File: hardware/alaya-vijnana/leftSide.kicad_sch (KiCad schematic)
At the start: 45 parts, among them J1 Bat, J2 USB_C_Receptacle_USB2.0_16P, U1 nRF52840, U2 BQ24075RGT, U3 XC6220B331MR, X1 32.768kHz, Y1 32Mhz

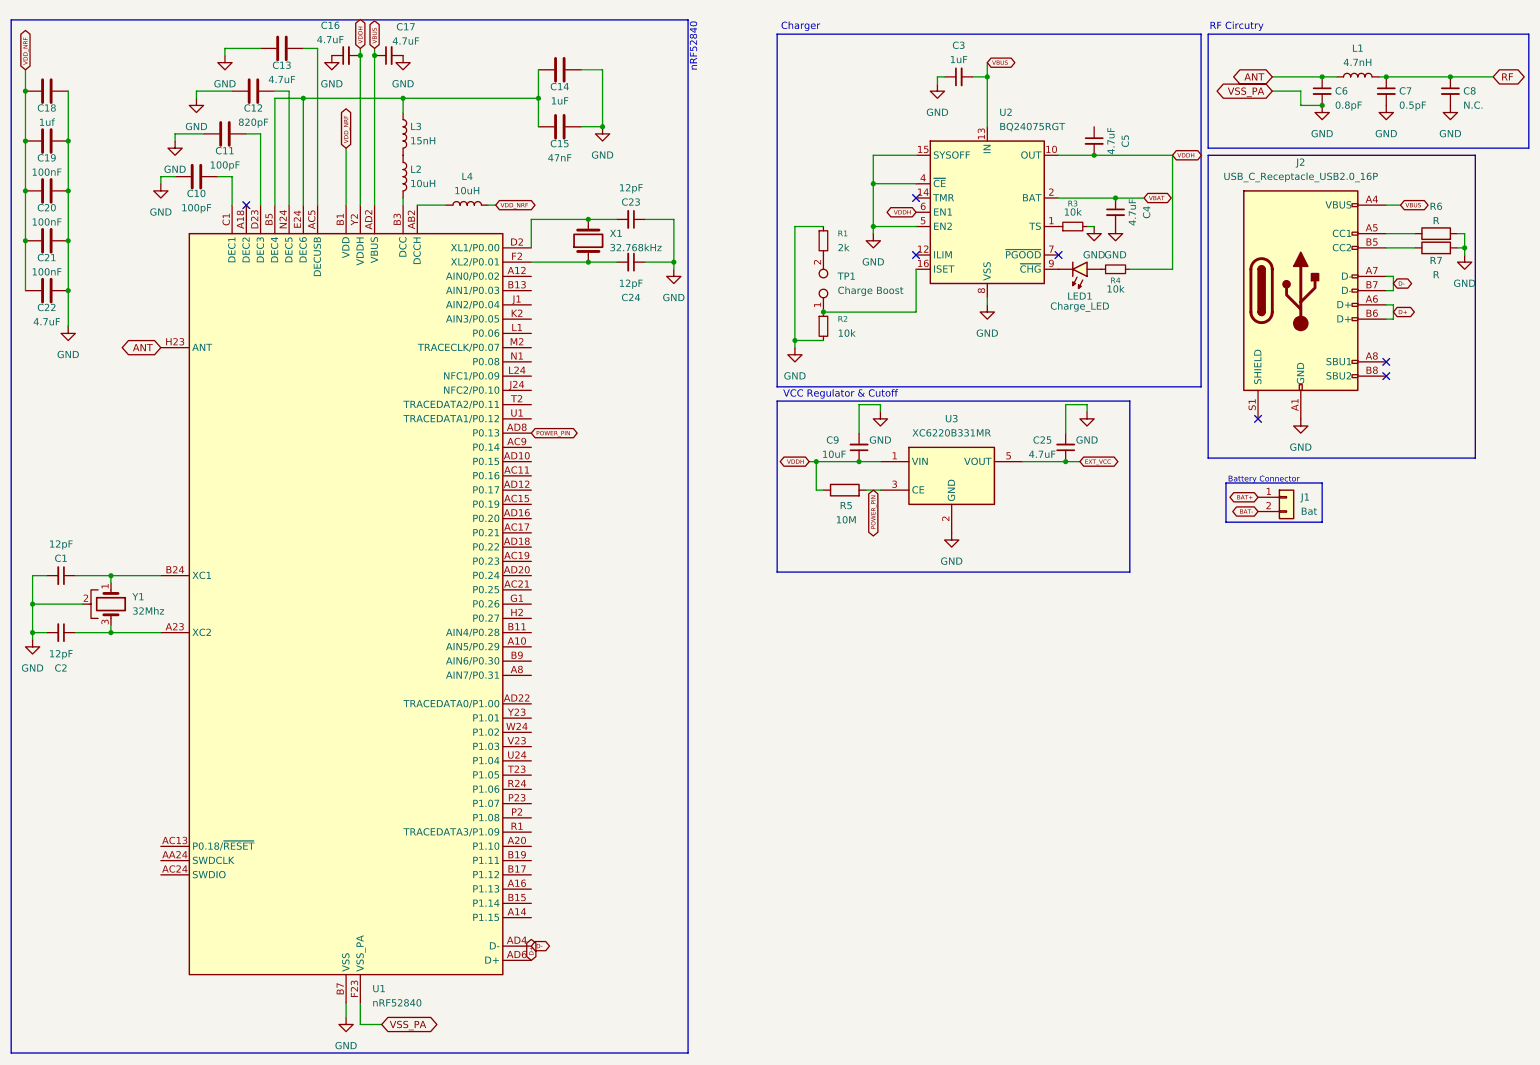
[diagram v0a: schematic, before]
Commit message: schematics done outside of cluster to main connectors, PCB laid out
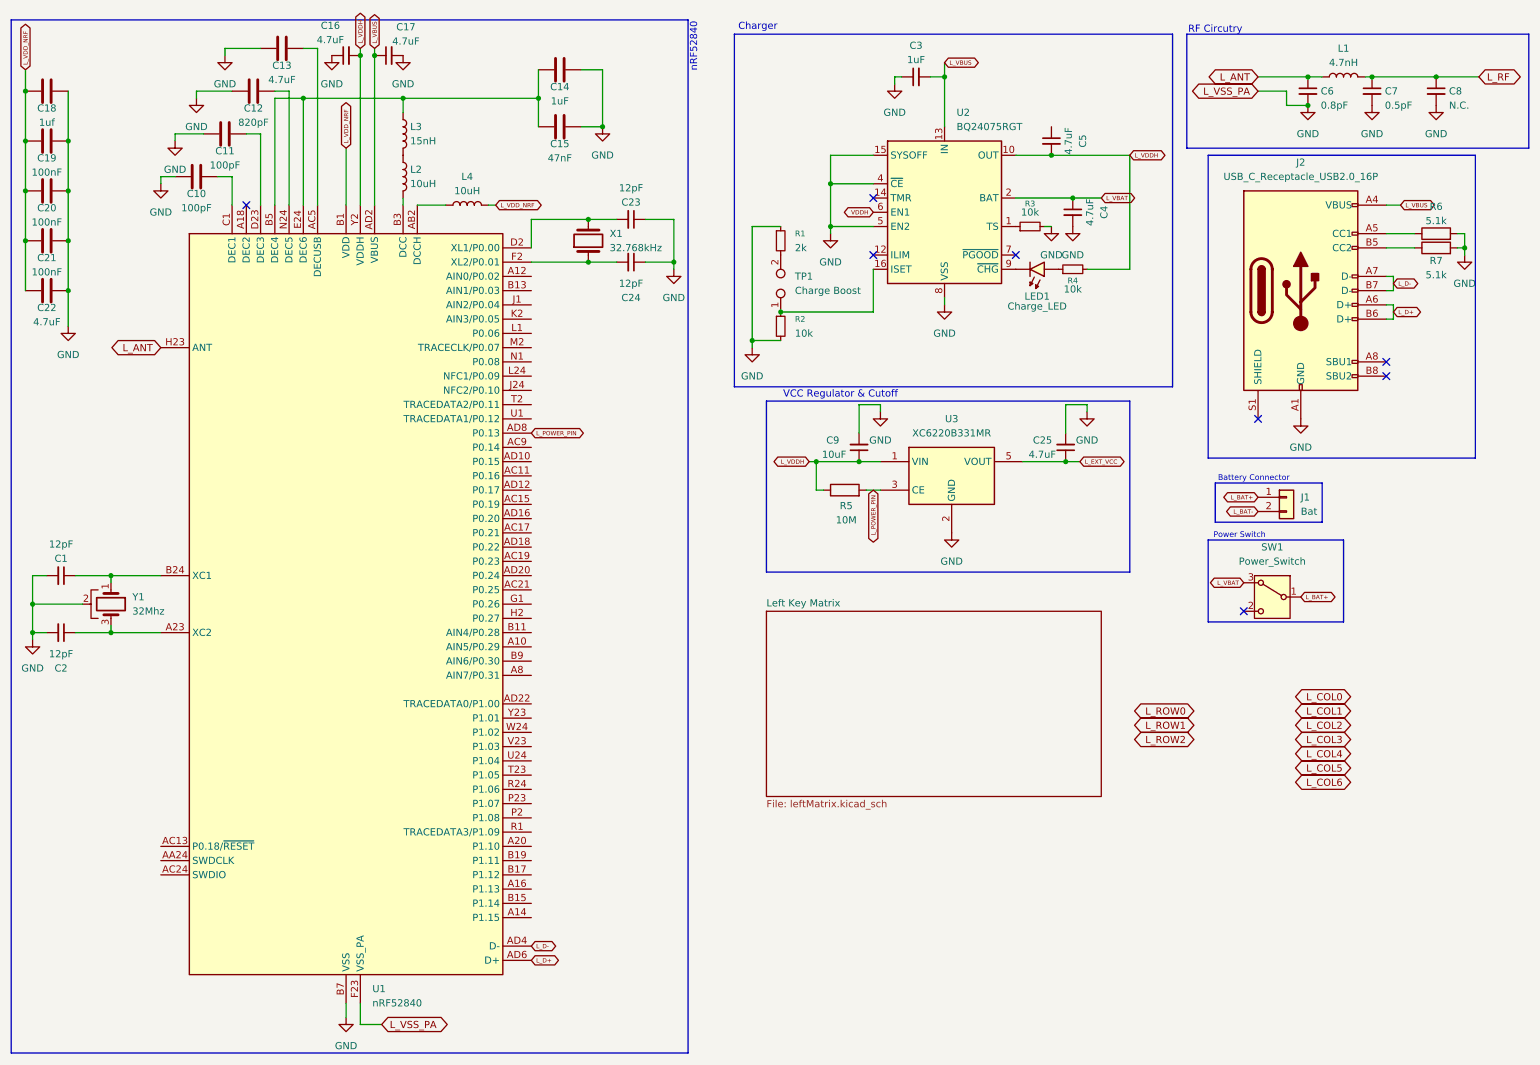
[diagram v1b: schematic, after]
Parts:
- added SW1: Power_Switch, Button_Switch_THT:SW_E-Switch_EG1224_SPDT_Angled, symbol Switch:SW_Wuerth_450301014042
- C1, C10, C11, C12, C13, C14, C15, C16, C17, C18, C19, C2, C20, C21, C22, C23, C24, C25, C3, C4, C5, C6, C7, C8, C9: footprint (none) -> Capacitor_SMD:C_0603_1608Metric_Pad1.08x0.95mm_HandSolder
- J2: footprint (none) -> Connector_USB:USB_C_Receptacle_GCT_USB4085
- L1: footprint (none) -> Inductor_SMD:L_0402_1005Metric_Pad0.77x0.64mm_HandSolder
- L2, L3, L4: footprint (none) -> Inductor_SMD:L_0603_1608Metric
- R1, R2, R3, R4, R5: footprint (none) -> Resistor_SMD:R_0603_1608Metric_Pad0.98x0.95mm_HandSolder
- R6, R7: value R -> 5.1k; footprint (none) -> Resistor_SMD:R_0603_1608Metric_Pad0.98x0.95mm_HandSolder
- TP1: footprint Connector_PinHeader_2.00mm:PinHeader_1x02_P2.00mm_Horizontal -> Resistor_SMD:R_2816_7142Metric_Pad3.20x4.45mm_HandSolder
- X1: footprint (none) -> Crystal:Crystal_SMD_2012-2Pin_2.0x1.2mm
- Y1: footprint (none) -> Crystal:Crystal_SMD_3225-4Pin_3.2x2.5mm_HandSoldering
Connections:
- net VDDH: no longer C16.2, C5.2, C9.1, R4.2, R5.1, U1.Y2 (VDDH), U2.10 (OUT), U2.11 (OUT), U3.1 (VIN)
- net ANT renamed L_ANT
- net BAT+ renamed L_BAT+
- net L_BAT+: now also SW1.1 (B)
- net BAT- renamed L_BAT-
- net D+ renamed L_D+
- net D- renamed L_D-
- net EXT_VCC renamed L_EXT_VCC
- net POWER_PIN renamed L_POWER_PIN
- net RF renamed L_RF
- net VBAT renamed L_VBAT
- net L_VBAT: now also SW1.3 (A)
- net VBUS renamed L_VBUS
- net VDD_NRF renamed L_VDD_NRF
- new net L_VDDH: C16.2, C5.2, C9.1, R4.2, R5.1, U1.Y2 (VDDH), U2.10 (OUT), U2.11 (OUT), U3.1 (VIN)
- no-connect marks 7 -> 8
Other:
- added sheet Left Key Matrix (leftMatrix.kicad_sch)
- note added: "Power Switch"
- moved on the sheet: C3, C4, C5, C6, C7, C8, L1, LED1, R1, R2, R3, R4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

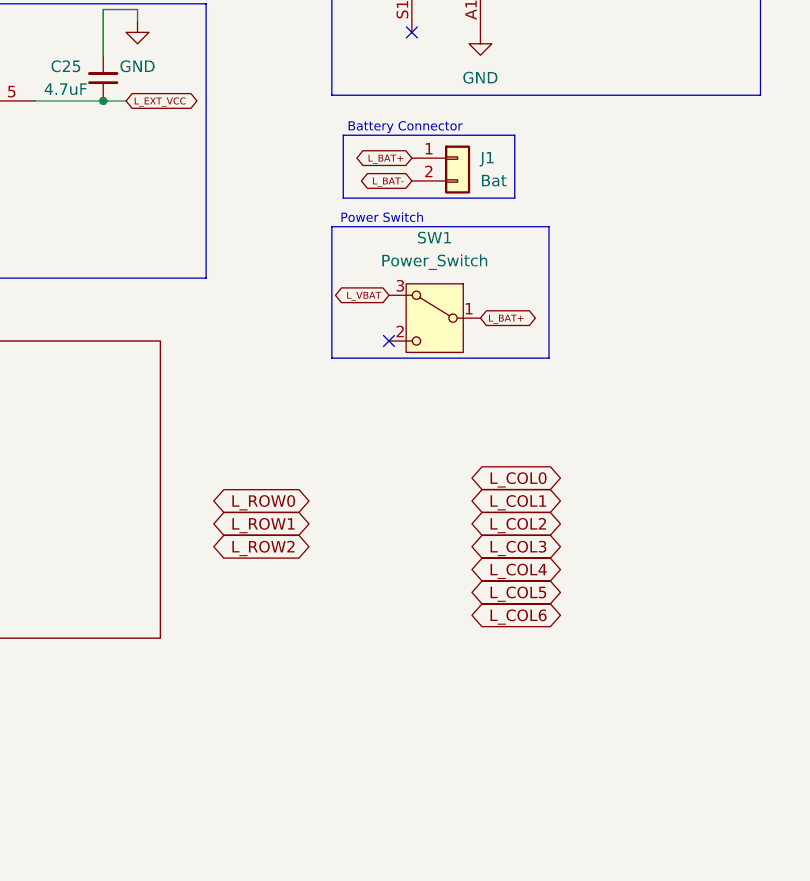
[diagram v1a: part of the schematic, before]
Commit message: finished key wiring w/ connectors
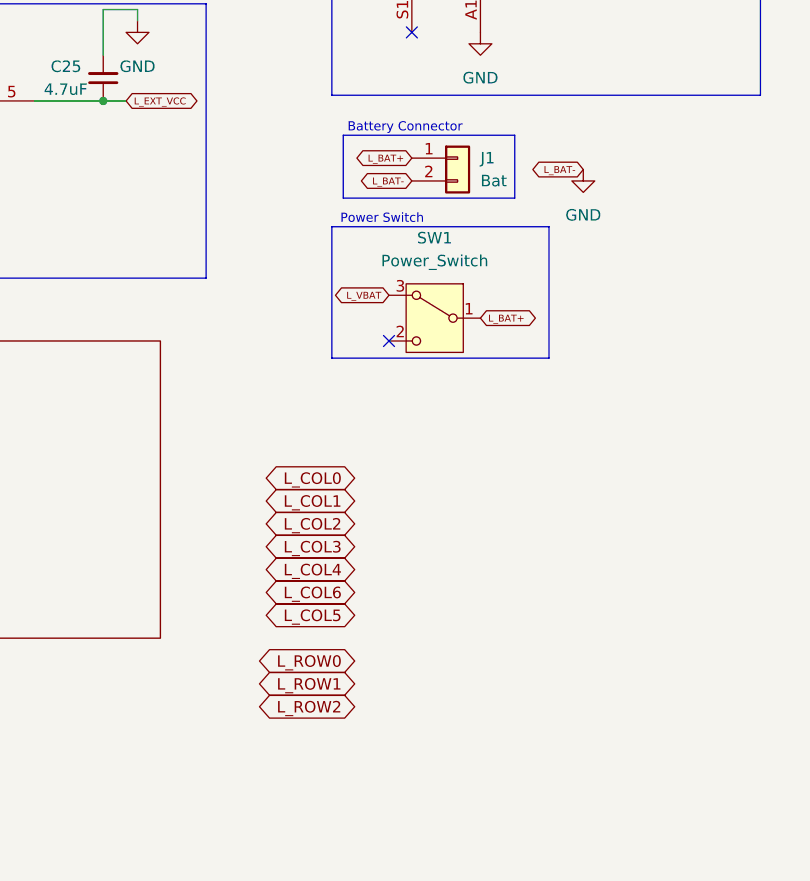
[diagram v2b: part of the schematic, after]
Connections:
- net L_BAT- is gone; now on net GND: J1.2 (Pin_2)
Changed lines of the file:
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@@
 		)
 	)
-	(global_label "L_ROW1"
+	(global_label "L_POWER_PIN"
 		(shape bidirectional)
-		(at 223.52 138.43 180)
+		(at 166.37 96.52 270)
 		(fields_autoplaced yes)
 		(effects
 			(font
-				(size 1.27 1.27)
+				(size 0.762 0.762)
 			)
 			(justify right)
 		)
 		(property "Intersheetrefs" "${INTERSHEET_REFS}"
-			(at 212.1664 138.43 0)
+			(at 166.37 106.5621 90)
 			(effects
 				(font
@@
 		)
 	)
-	(global_label "L_COL5"
+	(global_label "L_VDDH"
 		(shape bidirectional)
-		(at 251.46 146.05 180)
+		(at 212.09 36.83 0)
 		(fields_autoplaced yes)
 		(effects
 			(font
-				(size 1.27 1.27)
+				(size 0.762 0.762)
 			)
-			(justify right)
+			(justify left)
 		)
 		(property "Intersheetrefs" "${INTERSHEET_REFS}"
-			(at 240.5297 146.05 0)
+			(at 218.7211 36.83 0)
 			(effects
 				(font
 					(size 1.27 1.27)
 				)
-				(justify right)
+				(justify left)
 				(hide yes)
 			)
 		)
 	)
-	(global_label "L_POWER_PIN"
+	(global_label "L_ROW2"
 		(shape bidirectional)
-		(at 166.37 96.52 270)
+		(at 228.6 158.75 180)
 		(fields_autoplaced yes)
 		(effects
 			(font
-				(size 0.762 0.762)
+				(size 1.27 1.27)
 			)
 			(justify right)
 		)
 		(property "Intersheetrefs" "${INTERSHEET_REFS}"
-			(at 166.37 106.5621 90)
+			(at 217.2464 158.75 0)
 			(effects
 				(font
@@
 		)
 	)
-	(global_label "L_VDDH"
-		(shape bidirectional)
-		(at 212.09 36.83 0)
-		(fields_autoplaced yes)
-		(effects
-			(font
-				(size 0.762 0.762)
-			)
-			(justify left)
-		)
-		(property "Intersheetrefs" "${INTERSHEET_REFS}"
-			(at 218.7211 36.83 0)
-			(effects
-				(font
-					(size 1.27 1.27)
-				)
-				(justify left)
-				(hide yes)
-			)
-		)
-	)
-	(global_label "L_COL6"
+	(global_label "L_ROW1"
 		(shape bidirectional)
-		(at 251.46 148.59 180)
+		(at 228.6 156.21 180)
 		(fields_autoplaced yes)
 		(effects
@@
 		)
 		(property "Intersheetrefs" "${INTERSHEET_REFS}"
-			(at 240.5297 148.59 0)
+			(at 217.2464 156.21 0)
 			(effects
 				(font
@@
 		)
 	)
+	(global_label "L_COL6"
+		(shape bidirectional)
+		(at 228.6 146.05 180)
+		(fields_autoplaced yes)
+		(effects
+			(font
+				(size 1.27 1.27)
+			)
+			(justify right)
+		)
+		(property "Intersheetrefs" "${INTERSHEET_REFS}"
+			(at 217.6697 146.05 0)
+			(effects
+				(font
+					(size 1.27 1.27)
+				)
+				(justify right)
+				(hide yes)
+			)
+		)
+	)
+	(global_label "L_COL5"
+		(shape bidirectional)
+		(at 228.6 148.59 180)
+		(fields_autoplaced yes)
+		(effects
+			(font
+				(size 1.27 1.27)
+			)
+			(justify right)
+		)
+		(property "Intersheetrefs" "${INTERSHEET_REFS}"
+			(at 217.6697 148.59 0)
+			(effects
+				(font
+					(size 1.27 1.27)
+				)
+				(justify right)
+				(hide yes)
+			)
+		)
+	)
+	(global_label "L_BAT-"
+		(shape bidirectional)
+		(at 254 99.06 180)
+		(fields_autoplaced yes)
+		(effects
+			(font
+				(size 0.762 0.762)
+			)
+			(justify right)
+		)
+		(property "Intersheetrefs" "${INTERSHEET_REFS}"
+			(at 247.4052 99.06 0)
+			(effects
+				(font
+					(size 1.27 1.27)
+				)
+				(justify right)
+				(hide yes)
+			)
+		)
+	)
 	(global_label "L_ANT"
 		(shape bidirectional)
@@
 	(global_label "L_COL1"
 		(shape bidirectional)
-		(at 251.46 135.89 180)
+		(at 228.6 135.89 180)
 		(fields_autoplaced yes)
 		(effects
@@
 		)
 		(property "Intersheetrefs" "${INTERSHEET_REFS}"
-			(at 240.5297 135.89 0)
+			(at 217.6697 135.89 0)
 			(effects
 				(font
@@
 	(global_label "L_COL2"
 		(shape bidirectional)
-		(at 251.46 138.43 180)
+		(at 228.6 138.43 180)
 		(fields_autoplaced yes)
 		(effects
@@
 		)
 		(property "Intersheetrefs" "${INTERSHEET_REFS}"
-			(at 240.5297 138.43 0)
+			(at 217.6697 138.43 0)
 			(effects
 				(font
@@
 		)
 	)
-	(global_label "L_ROW0"
-		(shape bidirectional)
-		(at 223.52 135.89 180)
-		(fields_autoplaced yes)
-		(effects
-			(font
-				(size 1.27 1.27)
-			)
-			(justify right)
-		)
-		(property "Intersheetrefs" "${INTERSHEET_REFS}"
-			(at 212.1664 135.89 0)
-			(effects
-				(font
-					(size 1.27 1.27)
-				)
-				(justify right)
-				(hide yes)
-			)
-		)
-	)
 	(global_label "L_VSS_PA"
 		(shape bidirectional)
@@
 	(global_label "L_COL0"
 		(shape bidirectional)
-		(at 251.46 133.35 180)
+		(at 228.6 133.35 180)
 		(fields_autoplaced yes)
 		(effects
@@
 		)
 		(property "Intersheetrefs" "${INTERSHEET_REFS}"
-			(at 240.5297 133.35 0)
+			(at 217.6697 133.35 0)
 			(effects
 				(font
@@
 		)
 	)
-	(global_label "L_ROW2"
-		(shape bidirectional)
-		(at 223.52 140.97 180)
-		(fields_autoplaced yes)
-		(effects
-			(font
-				(size 1.27 1.27)
-			)
-			(justify right)
-		)
-		(property "Intersheetrefs" "${INTERSHEET_REFS}"
-			(at 212.1664 140.97 0)
-			(effects
-				(font
-					(size 1.27 1.27)
-				)
-				(justify right)
-				(hide yes)
-			)
-		)
-	)
 	(global_label "L_EXT_VCC"
 		(shape bidirectional)
@@
 	(global_label "L_COL3"
 		(shape bidirectional)
-		(at 251.46 140.97 180)
+		(at 228.6 140.97 180)
 		(fields_autoplaced yes)
 		(effects
@@
 		)
 		(property "Intersheetrefs" "${INTERSHEET_REFS}"
-			(at 240.5297 140.97 0)
+			(at 217.6697 140.97 0)
 			(effects
 				(font
@@
 		)
 	)
+	(global_label "L_ROW0"
+		(shape bidirectional)
+		(at 228.6 153.67 180)
+		(fields_autoplaced yes)
+		(effects
+			(font
+				(size 1.27 1.27)
+			)
+			(justify right)
+		)
+		(property "Intersheetrefs" "${INTERSHEET_REFS}"
+			(at 217.2464 153.67 0)
+			(effects
+				(font
+					(size 1.27 1.27)
+				)
+				(justify right)
+				(hide yes)
+			)
+		)
+	)
 	(global_label "L_COL4"
 		(shape bidirectional)
-		(at 251.46 143.51 180)
+		(at 228.6 143.51 180)
 		(fields_autoplaced yes)
 		(effects
@@
 		)
 		(property "Intersheetrefs" "${INTERSHEET_REFS}"
-			(at 240.5297 143.51 0)
+			(at 217.6697 143.51 0)
 			(effects
 				(font
@@
 					(unit 1)
 				)
+			)
+		)
+	)
+	(symbol
+		(lib_id "power:GND")
+		(at 254 99.06 0)
+		(unit 1)
+		(exclude_from_sim no)
+		(in_bom yes)
+		(on_board yes)
+		(dnp no)
+		(fields_autoplaced yes)
+		(property "Reference" "#PWR051"
+			(at 254 105.41 0)
+			(effects
+				(font
+					(size 1.27 1.27)
+				)
+				(hide yes)
+			)
+		)
+		(property "Value" "GND"
+			(at 254 104.14 0)
+			(effects
+				(font
+					(size 1.27 1.27)
+				)
+			)
+		)
+		(property "Footprint" ""
+			(at 254 99.06 0)
+			(effects
+				(font
+					(size 1.27 1.27)
+				)
+				(hide yes)
+			)
+		)
+		(property "Datasheet" ""
+			(at 254 99.06 0)
+			(effects
+				(font
+					(size 1.27 1.27)
+				)
+				(hide yes)
+			)
+		)
+		(property "Description" "Power symbol creates a global label with name \"GND\" , ground"
+			(at 254 99.06 0)
+			(effects
+				(font
+					(size 1.27 1.27)
+				)
+				(hide yes)
+			)
+		)
+		(pin "1"
+		)
+		(instances
+			(project ""
+				(path "/a3984b5f-5482-487c-827c-93986b80e1c8/0dccec26-d854-49d3-8867-bf55eaef7f97"
+					(reference "#PWR051")
+					(unit 1)
+				)
